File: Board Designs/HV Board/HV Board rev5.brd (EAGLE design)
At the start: 205 x 64.3 mm, 95 parts, among them IC1 OKI-78SR, IC2 NE5532SOIC, IC3 NE5532SOIC

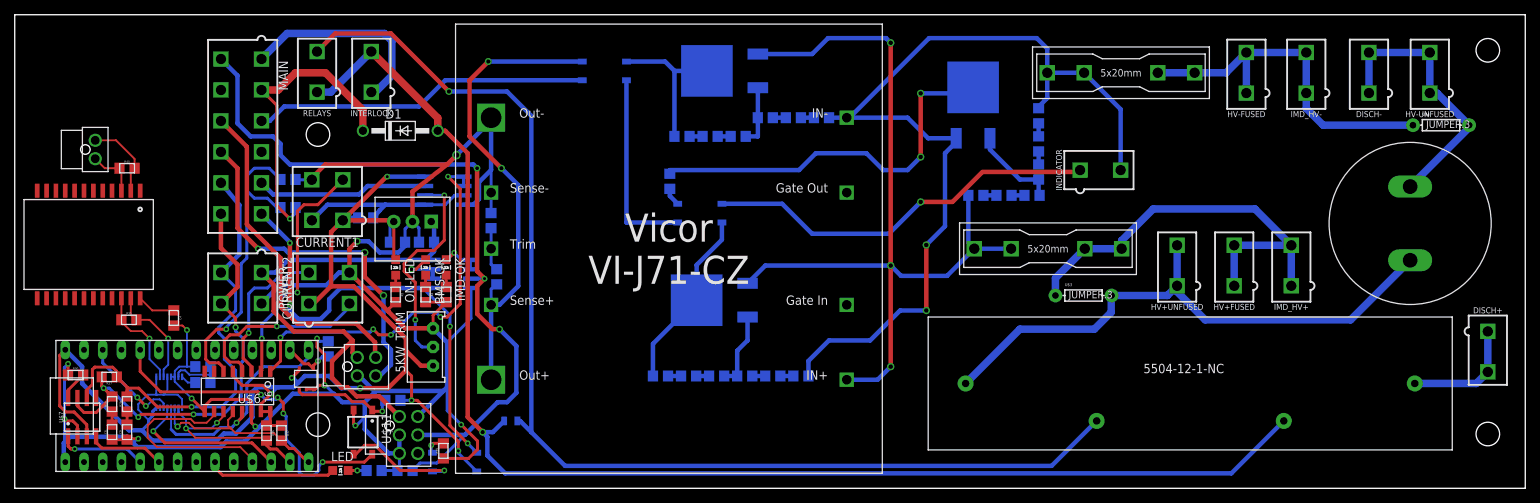
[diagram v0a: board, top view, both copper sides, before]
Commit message: HV board redesign
Removed one SSR in BMS, BSPD current sensor, jumper for fused/unfused, TSAL 60Vmin circuit, accumulator indicator, and energy meter connector. Connected output of DC/DC converter straight to TSAL out. Added 8th order butterworth filter to current sensor, replaced some mini-fit connectors to nano-fit.
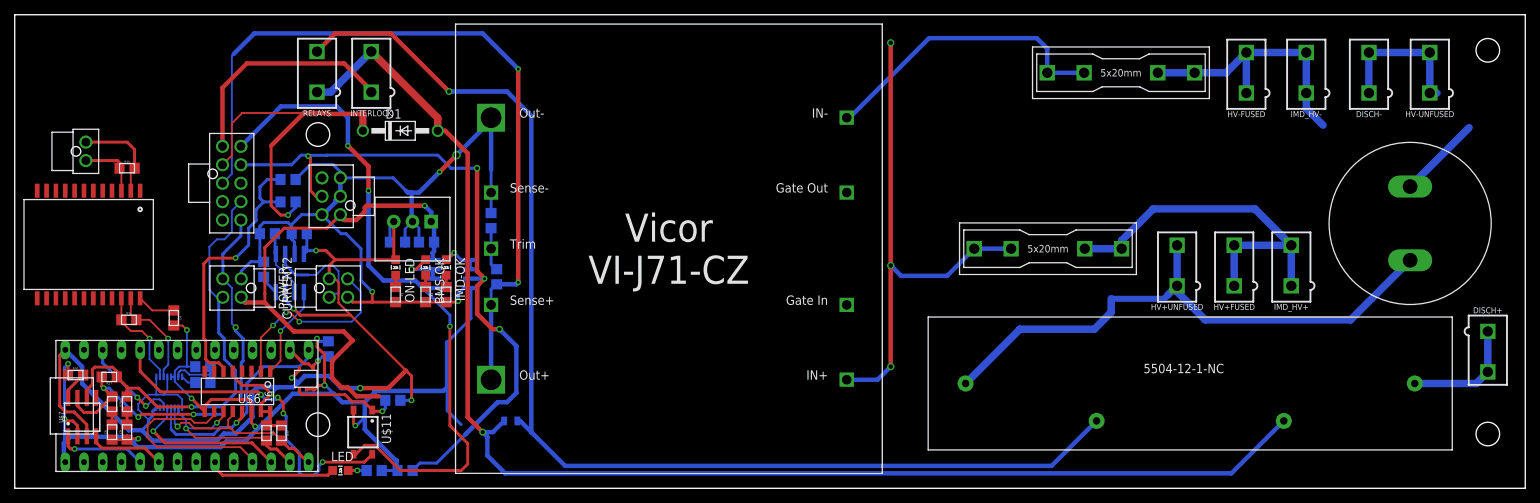
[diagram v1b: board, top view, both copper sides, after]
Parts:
- removed 5KW_TRIM: (no value), HyTechDevices:TRIMPOT_3296
- removed AI_SSR, TSAL_SSR: CPC1002N, HyTechDevices:SOP04
- removed CURRENT1: CONNECTOR-4, HyTechDevices:MINIFIT_5566-4
- removed EM: CONNECTOR-4, HyTechDevices:NANO-FIT_VERTICAL-4
- removed HV_REG1, HV_REG2: LR8, HyTechDevices:TO-252
- removed IC3: NE5532SOIC, HyTechDevices:SOIC-08
- removed INDICATOR: INDICATOR, HyTechDevices:MINIFIT_5566-2
- removed ISOSPI: CONNECTOR-2, HyTechDevices:NANO-FIT_VERTICAL-2
- removed R10, R8, R9: 8.2k, HyTechDevices:0805
- removed R11, R12, R13, R23, R24, R25: 2k, HyTechDevices:0805
- removed R14, R15, R16: 510k, HyTechDevices:0805
- removed R17, R18, R19: 43k, HyTechDevices:0805
- removed R20, R21, R22: 20k, HyTechDevices:0805
- removed R26: 1k, HyTechDevices:0805
- removed R39: 200, HyTechDevices:0805
- removed R6: 10k, HyTechDevices:0805
- removed THRESHOLD: AOD1N60, HyTechDevices:TO-252
- removed U$3, U$4: JUMPER.3, HyTechDevices:AXIAL-0.3
- added C5, C6: 0.1uF, HyTechDevices:0805
- added C7: 53pF, HyTechDevices:0805
- added ISO_SPI: CONNECTOR-2NANO-FIT_VERTICAL-2, HyTechDevices:NANO-FIT_VERTICAL-2
- CURRENT2, POWER: value CONNECTOR-4 -> CONNECTOR-4NANO-FIT-VERTICAL-4; device HyTechDevices:MINIFIT_5566-4 -> HyTechDevices:NANO-FIT_VERTICAL-4
- HV-UNFUSED: value FSAE -> HV_UNFUSED
- IMD: value CONNECTOR-6 -> CONNECTOR-6NANO-FIT_VERTICAL-6
- MAIN: value CONNECTOR-12 -> CONNECTOR-10NANO-FIT_VERTICAL-10; device HyTechDevices:MINIFIT_5566-12 -> HyTechDevices:NANO-FIT_VERTICAL-10
- U$1: device HyTechDevices:SOP04 -> HyTechDevices:SOIC-08
- moved U$1 34.0 mm to (37.3, 29.2), turned to 180 degrees
- moved IMD 33.4 mm to (44.2, 39.6), turned to 90 degrees
- moved MAIN 6.84 mm to (28.2, 41.4), turned to 270 degrees
- moved R1 0.76 mm to (37.1, 38.9)
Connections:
- removed net 5KW_TRIG: 5KW_TRIM.2, IC3.6
- removed net BMS_WATCH: U$1.1, U$11.3
- removed net BSPD_CUR_FAULT: IC3.7, MAIN.5
- removed net CUR_SENSE_1: IC3.1, IC3.2, U$6.1
- removed net CUR_SENSE_1_RAW: CURRENT1.2, IC3.3, IC3.5, R6.2
- removed net CUR_SENSE_2: CURRENT2.2, U$6.3
- removed net EM_IO1: EM.P$3, MAIN.9
- removed net EM_IO2: EM.P$4, MAIN.10
- removed net N$10: R14.1, R15.1
- removed net N$11: R15.2, R16.2
- removed net N$12: R17.1, R18.1
- removed net N$13: R18.2, R19.2
- removed net N$14: R10.2, R9.2
- removed net N$15: HV_REG2.3, R22.1, R23.1
- removed net N$16: R11.2, R12.2
- removed net N$17: R12.1, R13.1
- removed net N$18: HV_REG1.3, R10.1, R11.1
- removed net N$19: R23.2, R24.2
- removed net N$20: R24.1, R25.1
- removed net N$21: R21.2, R22.2
- removed net N$22: R16.1, R17.2, THRESHOLD.1
- removed net N$23: R20.1, R21.1
- removed net N$5: AI_SSR.2, R26.1
- removed net N$6: AI_SSR.1, TSAL_SSR.2
- removed net N$7: AI_SSR.3, INDICATOR.1
- removed net N$8: R8.1, R9.1
- removed net N$9: R26.2, THRESHOLD.2(TAB)
- removed net TEMP_SENSE_1: CURRENT1.3, U$6.2
- removed net TEMP_SENSE_2: CURRENT2.3, U$6.4
- removed net TSAL_1: TRIM+.2, TSAL_SSR.4, U$5.5VOUT+, U$5.6SENSE+
- new net CUR_SENSE: CURRENT2.P$2, U$1.2
- new net TEMP_SENSE: CURRENT2.P$3, U$6.2
- net +12V: now also POWER.P$1; no longer EM.P$1, POWER.1
- net +5V: now also C5.1, CURRENT2.P$1, U$1.7; no longer 5KW_TRIM.1, CURRENT1.1, CURRENT2.1, IC3.8, R6.1
- net BMS_OK: now also MAIN.P$6, U$11.3; no longer MAIN.6, U$1.3
- net CANH: now also MAIN.P$10, POWER.P$4; no longer MAIN.12, POWER.4
- net CANL: now also MAIN.P$9, POWER.P$3; no longer MAIN.11, POWER.3
- net GND: now also C5.2, C6.2, C7.2, CURRENT2.P$4, POWER.P$2, U$1.3; no longer 5KW_TRIM.3, CURRENT1.4, CURRENT2.4, EM.P$2, IC3.4, POWER.2, R39.1
- net HV+FUSED: no longer U$3.P$1
- net HV+FUSED_1A: no longer HV_REG1.1, HV_REG2.1, R14.2
- net HV+UNFUSED_FSAE: no longer U$3.P$2
- net HV-FUSED: no longer U$4.P$1
- net HV-FUSED_1A: no longer INDICATOR.2, R19.1, R20.2, R8.2, THRESHOLD.3
- net HV-UNFUSED_FSAE: no longer U$4.P$2
- net ISOSPI-M: now also ISO_SPI.P$2; no longer ISOSPI.P$2
- net ISOSPI-P: now also ISO_SPI.P$1; no longer ISOSPI.P$1
- net N$1: now also U$1.5, U$6.1; no longer AI_SSR.4, HV_REG2.2(TAB), R25.2
- net N$2: now also C6.1, U$1.1, U$1.6; no longer HV_REG1.2(TAB), R13.2, TSAL_SSR.1
- net N$4: now also C7.1, U$1.8; no longer R39.2, U$1.2
- net OKHS: now also MAIN.P$7; no longer MAIN.7
- net SHUTDOWN6: now also MAIN.P$1; no longer MAIN.1
- net SHUTDOWN7_EXT_OUT: now also MAIN.P$2; no longer MAIN.2
- net TSAL+: now also MAIN.P$3, TRIM+.2, U$5.5VOUT+, U$5.6SENSE+; no longer MAIN.3, TSAL_SSR.3
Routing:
- net HV-FUSED_1A: track 125.1 -> 40.5 mm, vias 2 -> 0
- net TSAL_1: track 65.1 -> 0.00 mm, vias 2 -> 0
- net TSAL+: track 45.8 -> 105.2 mm, vias 0 -> 2
- net CUR_SENSE_1: track 53.9 -> 0.00 mm, vias 5 -> 0
- net N$7: track 53.9 -> 0.00 mm, vias 1 -> 0
- net N$9: track 53.2 -> 0.00 mm, vias 2 -> 0
- net EM_IO2: track 49.3 -> 0.00 mm, vias 3 -> 0
- net HV+FUSED_1A: track 116.3 -> 70.2 mm
- net EM_IO1: track 45.5 -> 0.00 mm
- net TEMP_SENSE_1: track 32.5 -> 0.00 mm, vias 2 -> 0
- net 5KW_TRIG: track 29.3 -> 0.00 mm, vias 2 -> 0
- net BMS_OK: track 63.1 -> 91.4 mm, vias 4 -> 3
- net N$6: track 26.3 -> 0.00 mm
- net TEMP_SENSE: track 0.00 -> 26.0 mm, vias 0 -> 3
- net TEMP_SENSE_2: track 25.2 -> 0.00 mm, vias 1 -> 0
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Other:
- board text added: "2018_hv_board_rev5"
- board text added: "Designed by Nathan Cheek, Yvonne Yeh"
- board text removed: "2018_hv_board_rev4"
- board text removed: "Designed by Nathan Cheek"
